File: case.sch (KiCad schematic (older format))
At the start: 1 part

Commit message: toslink reciever and transmitter
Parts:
- added C? (x7): 0.1, symbol C_Small
- added L?: INDUCTOR_SMALL, symbol INDUCTOR_SMALL
- added U? (x6): totx177, symbol totx177
- added U?: torx177, symbol torx177
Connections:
- net labels added: GND, Toslink_RX1, Toslink_RX2, Toslink_RX3, Toslink_RX4, Toslink_RX5, Toslink_RX6, Toslink_TX1, VCC
- wire segments 3 -> 57

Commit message: Odroid
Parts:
- added 47k: R, symbol R
- added S? (x2): dip, symbol dip
- added U?: PCF8574, symbol PCF8574
- added U?: ULN2003A, symbol ULN2003A
- L?: value INDUCTOR_SMALL -> 47µH
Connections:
- net labels added: SCL, SDA
- wire segments 57 -> 91
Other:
- moved on the sheet: C?, L?, U?

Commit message: Weiterentwicklung des Netzteiles
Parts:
- removed S?: switch, symbol switch
- added X?: IEC_power, symbol IEC_power
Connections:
- net labels added: 5V_MAIN, L_O, N_O
- net labels removed: GND_preamp, PE_I, VCC
- wire segments 91 -> 131
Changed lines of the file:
@@
 $Descr A4 11693 8268
 encoding utf-8
-Sheet 5 8
+Sheet 12 12
 Title ""
 Date ""
@@
 Comment4 ""
 $EndDescr
-Text HLabel 2800 1575 0    60   Output ~ 0
-PE_I
 $Comp
 L Earth #PWR?
 U 1 1 5883EA93
-P 3050 1775
-F 0 "#PWR?" H 3050 1525 50  0001 C CNN
-F 1 "Earth" H 3050 1625 50  0001 C CNN
-F 2 "" H 3050 1775 50  0000 C CNN
-F 3 "" H 3050 1775 50  0000 C CNN
-	1    3050 1775
+P 2175 1175
+F 0 "#PWR?" H 2175 925 50  0001 C CNN
+F 1 "Earth" H 2175 1025 50  0001 C CNN
+F 2 "" H 2175 1175 50  0000 C CNN
+F 3 "" H 2175 1175 50  0000 C CNN
+	1    2175 1175
 	1    0    0    -1
 $EndComp
-$Comp
-L switch S?
-U 1 1 5883EC68
-P 3150 1575
-F 0 "S?" H 3200 1690 60  0000 C CNN
-F 1 "switch" H 3285 1520 60  0000 C CNN
-F 2 "" H 3150 1575 60  0001 C CNN
-F 3 "" H 3150 1575 60  0001 C CNN
-	1    3150 1575
-	1    0    0    -1
-$EndComp
-Text HLabel 3500 1575 2    60   Input ~ 0
-GND_preamp
 $Comp
 L totx177 U?
@@
 GND
 Wire Wire Line
-	3050 1775 3050 1575
-Wire Wire Line
-	2800 1575 3150 1575
-Connection ~ 3050 1575
-Wire Wire Line
-	3500 1575 3425 1575
+	2175 1175 2175 975
+Wire Wire Line
+	2175 975  1750 975
 $Comp
 L totx177 U?
@@
 $EndComp
 Text HLabel 3050 2850 0    60   Output ~ 0
-VCC
+5V_MAIN
 $Comp
 L C_Small C?
@@
 $EndComp
 Wire Wire Line
-	3175 3825 5475 3825
+	3175 3825 3275 3825
+Wire Wire Line
+	3275 3825 3550 3825
+Wire Wire Line
+	3550 3825 5400 3825
+Wire Wire Line
+	5400 3825 5475 3825
 Wire Wire Line
 	3275 3825 3275 3875
@@
 	3050 2750 3550 2750
 Wire Wire Line
-	3550 2750 3550 5325
+	3550 2750 3550 3825
+Wire Wire Line
+	3550 3825 3550 4225
+Wire Wire Line
+	3550 4225 3550 4475
+Wire Wire Line
+	3550 4475 3550 5150
+Wire Wire Line
+	3550 5150 3550 5325
 Connection ~ 3275 3825
 Wire Wire Line
-	3175 4100 3450 4100
+	3175 4100 3275 4100
+Wire Wire Line
+	3275 4100 3450 4100
 Wire Wire Line
 	3275 4100 3275 4075
 Wire Wire Line
-	3450 5425 3450 2375
+	3450 5425 3450 4750
+Wire Wire Line
+	3450 4750 3450 4100
+Wire Wire Line
+	3450 4100 3450 2850
+Wire Wire Line
+	3450 2850 3450 2375
 Wire Wire Line
 	3450 2850 3050 2850
 Connection ~ 3275 4100
 Wire Wire Line
-	3175 4475 3550 4475
+	3175 4475 3275 4475
+Wire Wire Line
+	3275 4475 3550 4475
 Connection ~ 3550 3825
 Wire Wire Line
-	3175 5150 3550 5150
+	3175 5150 3275 5150
+Wire Wire Line
+	3275 5150 3550 5150
 Connection ~ 3550 4475
 Wire Wire Line
-	3550 5325 5150 5325
-Wire Wire Line
-	3675 5325 3675 5625
+	3550 5325 3675 5325
+Wire Wire Line
+	3675 5325 4425 5325
+Wire Wire Line
+	4425 5325 5150 5325
+Wire Wire Line
+	3675 5325 3675 5575
+Wire Wire Line
+	3675 5575 3675 5625
 Connection ~ 3550 5150
 Wire Wire Line
@@
 Connection ~ 3675 5575
 Wire Wire Line
-	3175 4750 3450 4750
+	3175 4750 3275 4750
+Wire Wire Line
+	3275 4750 3450 4750
 Connection ~ 3450 4100
 Wire Wire Line
-	3175 5425 5425 5425
+	3175 5425 3275 5425
+Wire Wire Line
+	3275 5425 3450 5425
+Wire Wire Line
+	3450 5425 3950 5425
+Wire Wire Line
+	3950 5425 4700 5425
+Wire Wire Line
+	4700 5425 5425 5425
 Connection ~ 3450 4750
 Wire Wire Line
@@
 Connection ~ 3275 5425
 Wire Wire Line
-	3950 5425 3950 5625
+	3950 5425 3950 5575
+Wire Wire Line
+	3950 5575 3950 5625
 Wire Wire Line
 	3950 5575 3925 5575
@@
 Connection ~ 3450 5425
 Wire Wire Line
-	4425 5325 4425 5625
+	4425 5325 4425 5575
+Wire Wire Line
+	4425 5575 4425 5625
 Connection ~ 3675 5325
 Wire Wire Line
-	5150 5325 5150 5625
+	5150 5325 5150 5575
+Wire Wire Line
+	5150 5575 5150 5625
 Connection ~ 4425 5325
 Wire Wire Line
-	4700 5425 4700 5625
+	4700 5425 4700 5575
+Wire Wire Line
+	4700 5575 4700 5625
 Connection ~ 3950 5425
 Wire Wire Line
-	5425 5425 5425 5625
+	5425 5425 5425 5575
+Wire Wire Line
+	5425 5575 5425 5625
 Connection ~ 4700 5425
 Wire Wire Line
@@
 	5400 3825 5400 3875
 Wire Wire Line
-	5100 4100 5475 4100
+	5100 4100 5400 4100
+Wire Wire Line
+	5400 4100 5475 4100
 Wire Wire Line
 	5400 4100 5400 4075
@@
 	8250 4225 8250 3925
 Wire Wire Line
-	3550 4225 9625 4225
+	3550 4225 6175 4225
+Wire Wire Line
+	6175 4225 8250 4225
+Wire Wire Line
+	8250 4225 9400 4225
+Wire Wire Line
+	9400 4225 9475 4225
+Wire Wire Line
+	9475 4225 9550 4225
+Wire Wire Line
+	9550 4225 9625 4225
 Connection ~ 3550 4225
 Wire Wire Line
@@
 Connection ~ 9550 4225
 Wire Wire Line
-	9400 2975 9400 3450
+	9400 2975 9400 3125
+Wire Wire Line
+	9400 3125 9400 3450
 Wire Wire Line
 	9400 3125 8750 3125
@@
 	8750 3325 9550 3325
 Wire Wire Line
-	9550 2975 9550 3450
+	9550 2975 9550 3325
+Wire Wire Line
+	9550 3325 9550 3450
 $Comp
 L dip S?
@@
 Connection ~ 9400 3125
 Wire Wire Line
-	9475 2975 9475 3450
+	9475 2975 9475 3225
+Wire Wire Line
+	9475 3225 9475 3450
 Connection ~ 9475 3225
 $Comp
@@
 $EndComp
 Wire Wire Line
-	3450 2375 8800 2375
-Wire Wire Line
-	9100 2375 9625 2375
+	3450 2375 8250 2375
+Wire Wire Line
+	8250 2375 8800 2375
+Wire Wire Line
+	9100 2375 9400 2375
+Wire Wire Line
+	9400 2375 9475 2375
+Wire Wire Line
+	9475 2375 9550 2375
+Wire Wire Line
+	9550 2375 9625 2375
+$Comp
+L IEC_power X?
+U 1 1 58BCF522
+P 1250 1075
+F 0 "X?" H 1300 1375 60  0000 C CNN
+F 1 "IEC_power" H 1475 1025 60  0000 C CNN
+F 2 "" H 1250 1075 60  0001 C CNN
+F 3 "" H 1250 1075 60  0001 C CNN
+	1    1250 1075
+	1    0    0    -1
+$EndComp
+Text HLabel 1900 900  2    60   Output ~ 0
+L_O
+Text HLabel 1900 1050 2    60   Input ~ 0
+N_O
+Wire Wire Line
+	1900 900  1700 900
+Wire Wire Line
+	1750 1050 1900 1050
 $EndSCHEMATC

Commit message: blub
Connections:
- net at S?.~: now also 47k.1; no longer S?.~
- new net: S?.~, S?.~, U?.1 (A0)
- new net: S?.~, S?.~, U?.2 (A1)
- new net: S?.~, S?.~, U?.3 (A2)
- new net: S?.~, S?.~
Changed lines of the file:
@@
 $Descr A4 11693 8268
 encoding utf-8
-Sheet 12 12
+Sheet 12 13
 Title ""
 Date ""

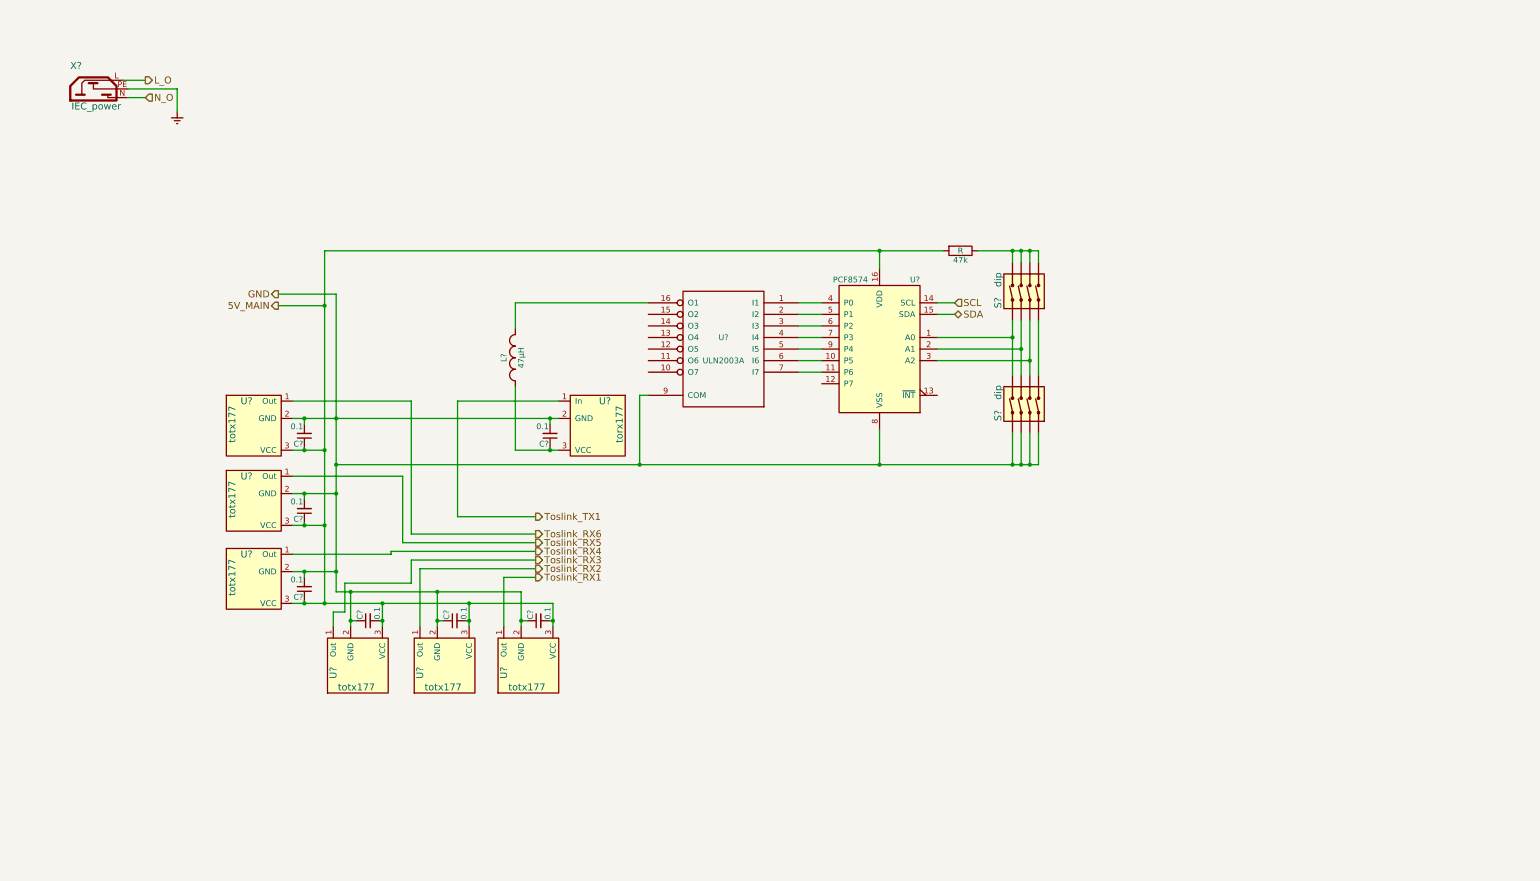
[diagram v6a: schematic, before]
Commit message: phono_preamp and more
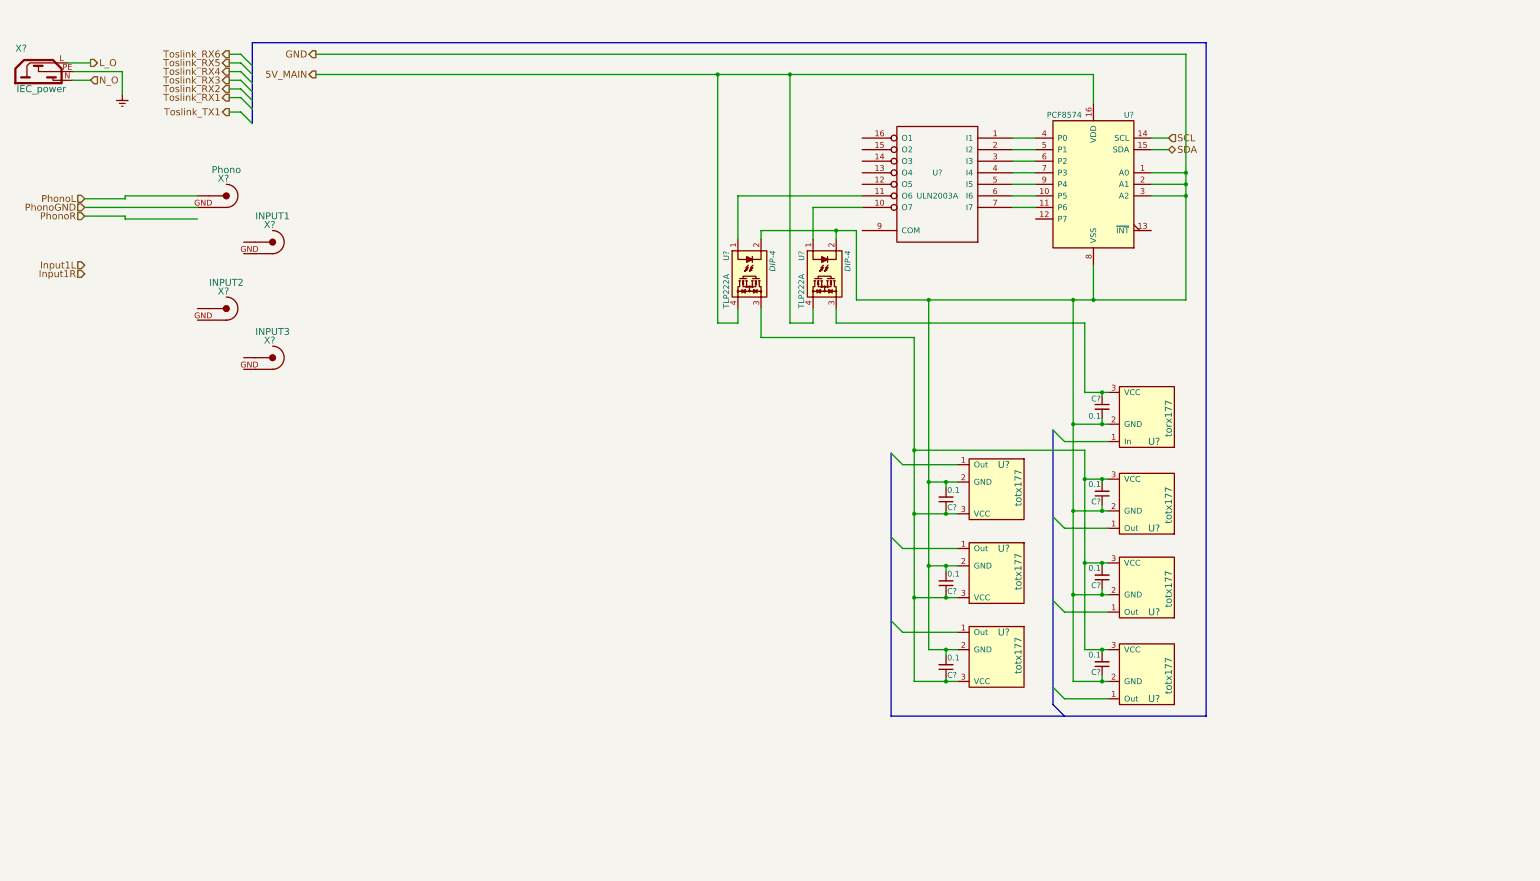
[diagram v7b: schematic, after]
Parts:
- removed 47k: R, symbol R
- removed L?: 47µH, symbol INDUCTOR_SMALL
- removed S? (x2): dip, symbol dip
- added U? (x2): TLP222A, DIP-4, symbol TLP222A
- added X?: Phono, symbol RCA
- added X?: INPUT1, symbol RCA
- added X?: INPUT2, symbol RCA
- added X?: INPUT3, symbol RCA
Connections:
- net 5V_MAIN: now also U?.4, U?.4; no longer C?.1, C?.1, C?.1, C?.2, C?.2, C?.2, U?.3 (VCC), U?.3 (VCC), U?.3 (VCC), U?.3 (VCC), U?.3 (VCC), U?.3 (VCC)
- net GND: now also U?.1 (A0), U?.2 (A1), U?.3 (A2), U?.2, U?.2; no longer U?.9 (COM)
- net Toslink_RX1: no longer U?.1 (Out)
- net Toslink_RX2: no longer U?.1 (Out)
- net Toslink_RX3: no longer U?.1 (Out)
- net Toslink_RX4: no longer U?.1 (Out)
- net Toslink_RX5: no longer U?.1 (Out)
- net Toslink_RX6: no longer U?.1 (Out)
- net Toslink_TX1: no longer U?.1 (In)
- net at U?.10 (O7): now also U?.1
- net at U?.11 (O6): now also U?.1
- net at C?.1, U?.3 (VCC): now also U?.3
- new net: C?.1, C?.1, C?.1, C?.2, C?.2, C?.2, U?.3, U?.3 (VCC), U?.3 (VCC), U?.3 (VCC), U?.3 (VCC), U?.3 (VCC), U?.3 (VCC)
- new net PhonoGND: X?.GND
- new net PhonoL: X?.~
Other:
- moved on the sheet: C?, U?, X?

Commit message: daily commit. Added new ADC
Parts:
- removed U? (x5): totx177, symbol totx177
- removed U? (x2): TLP222A, DIP-4, symbol TLP222A
- removed X?: Phono, symbol RCA
- removed X?: INPUT1, symbol RCA
- removed X?: INPUT2, symbol RCA
- removed X?: INPUT3, symbol RCA
- added K? (x10): RY12WK, symbol RY12WK
- added U?: GroundPost, symbol GroundPost
- added U? (x5): torx177, symbol torx177
- added X? (x2): PREOUT_L, symbol RCA
- added X? (x2): PREOUT_R, symbol RCA
- added X?: PHONO_L, symbol RCA
- added X?: PHONO_R, symbol RCA
- added X?: INPUT1_L, symbol RCA
- added X?: INPUT2_R, symbol RCA
- added X?: RJ45_extension, symbol RJ45_extension
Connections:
- net 5V_MAIN: now also U?.9 (COM), K?.4, K?.4
- net Earth: now also U?.~, X?.~
- net GND: now also K?.1, K?.1, K?.1, K?.1, K?.16, K?.16, K?.16, K?.16, U?.2 (GND), U?.2 (GND), U?.2 (GND), U?.2 (GND), U?.2 (GND)
- net PhonoL: now also K?.8
- net PhonoR: now also K?.9
- net SCL: no longer U?.14 (SCL)
- net SDA: no longer U?.15 (SDA)
- net VCC_Toslink_RX: now reaches C?.1, C?.1, C?.1, C?.2, C?.2, C?.2
- net VCC_Toslink_RX: now also U?.3 (VCC), K?.8, U?.3 (VCC), U?.3 (VCC), U?.3 (VCC), U?.3 (VCC), U?.3 (VCC); no longer U?.3 (VCC)
- net TOSLINK_TX1: now reaches U?.1 (Out)
- net TOSLINK_RX1: now reaches U?.1 (In)
- net VCC_Toslink_TX: now reaches C?.1
- net VCC_Toslink_TX: now also U?.3 (VCC), K?.8; no longer U?.3 (VCC)
- new net: K?.13, X?.GND (x4)
- new net: K?.4, X?.~ (x4)
- new net: K?.13, X?.~ (x4)
- new net: K?.4, X?.GND (x4)
- new net: K?.1, K?.16
- new net PhonoLGND: K?.9
- new net PhonoRGND: K?.8
- new net PreoutL: K?.8, K?.8, K?.8
- new net PreoutLGND: K?.8, K?.8, K?.9, K?.9, K?.9
- new net PreoutR: K?.9, K?.9, K?.9
- new net PreoutRGND: K?.8
- new net TOSLINK_RX2: U?.1 (In)
- new net TOSLINK_RX3: U?.1 (In)
- new net TOSLINK_RX4: U?.1 (In)
- new net TOSLINK_RX5: U?.1 (In)
- new net TOSLINK_RX6: U?.1 (In)
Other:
- moved on the sheet: C?, U?, X?
